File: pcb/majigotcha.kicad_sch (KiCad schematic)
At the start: 11 parts, among them SW1 SW_Push, SW2 SW_Push, SW3 SW_Push, U1 XIAO-ESP32-C6, U2 DM-OLED096-636, U3 TPP233-IC, U4 TOUCH CAPACITIVE

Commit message: finish the pcb
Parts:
- removed U1: XIAO-ESP32-C6, footprints:XIAO-Generic-Hybrid-14P-2.54-21X17.8MM, symbol Seeed_Studio_XIAO_Series:XIAO_ESP32-C6-DIP
- added U5: XIAO-ESP32-S3-SMD, Seeed Studio XIAO Series Library:XIAO-ESP32C6-SMD, symbol Seeed_Studio_XIAO_Series:XIAO-ESP32-C6-SMD
- BT1: footprint (none) -> Connector_PinHeader_2.54mm:PinHeader_1x02_P2.54mm_Vertical
- BUZZER1: footprint buzzer:C49246964_BUZ-TH_BD12_5-P6_50-D1_4 -> Buzzer_Beeper:Buzzer_TDK_PS1240P02BT_D12.2mm_H6.5mm
- SW1, SW2, SW3: footprint Button_Switch_THT:SW_PUSH_6mm -> Button_Switch_THT:SW_PUSH_6mm_H5mm
- U3: value TPP233-IC -> TPP233-capacitive; footprint DFR0299:MODULE_DFR0299 -> DFR0299:TTP223-CAPACITIVE
- U4: footprint sen0348:Untitled -> Connector_PinHeader_2.54mm:PinHeader_1x06_P2.54mm_Vertical
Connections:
- net +3V3: now also U5.12 (3V3)
- net +5V: now also U5.14 (5V)
- net BTN1: now also U5.2 (GPIO1_A1_D1)
- net BTN2: now also U5.1 (GPIO0_A0_D0)
- net BTN3: now also U5.10 (GPIO20_D9_MISO)
- net GND: now also BT1.2 (-), U3.3 (GND), U5.13 (GND), U5.16 (GND); no longer U3.7 (GND)
- net POTENTIO: now also U5.3 (GPIO2_A2_D2)
- net RX: now also U5.8 (GPIO17_D7_RX)
- net SCL: now also U5.6 (GPIO23_D5_SCL)
- net SDA: now also U5.5 (GPIO22_D4_SDA)
- net TOUCH: now also U3.2 (SIG/LOW), U5.4 (GPIO21_D3); no longer U3.9 (SIG/LOW)
- net TOUCH_OUT: now also U5.9 (GPIO19_D8_SCK)
- net TX: now also U5.7 (GPIO16_D6_TX)
- net +BATT: now reaches BT1.1 (+)
- net +BATT: now also U5.15 (BAT); no longer BT1.
- net BUZ: now reaches BUZZER1.1 (+)
- net BUZ: now also U5.11 (GPIO18_D10_MOSI)

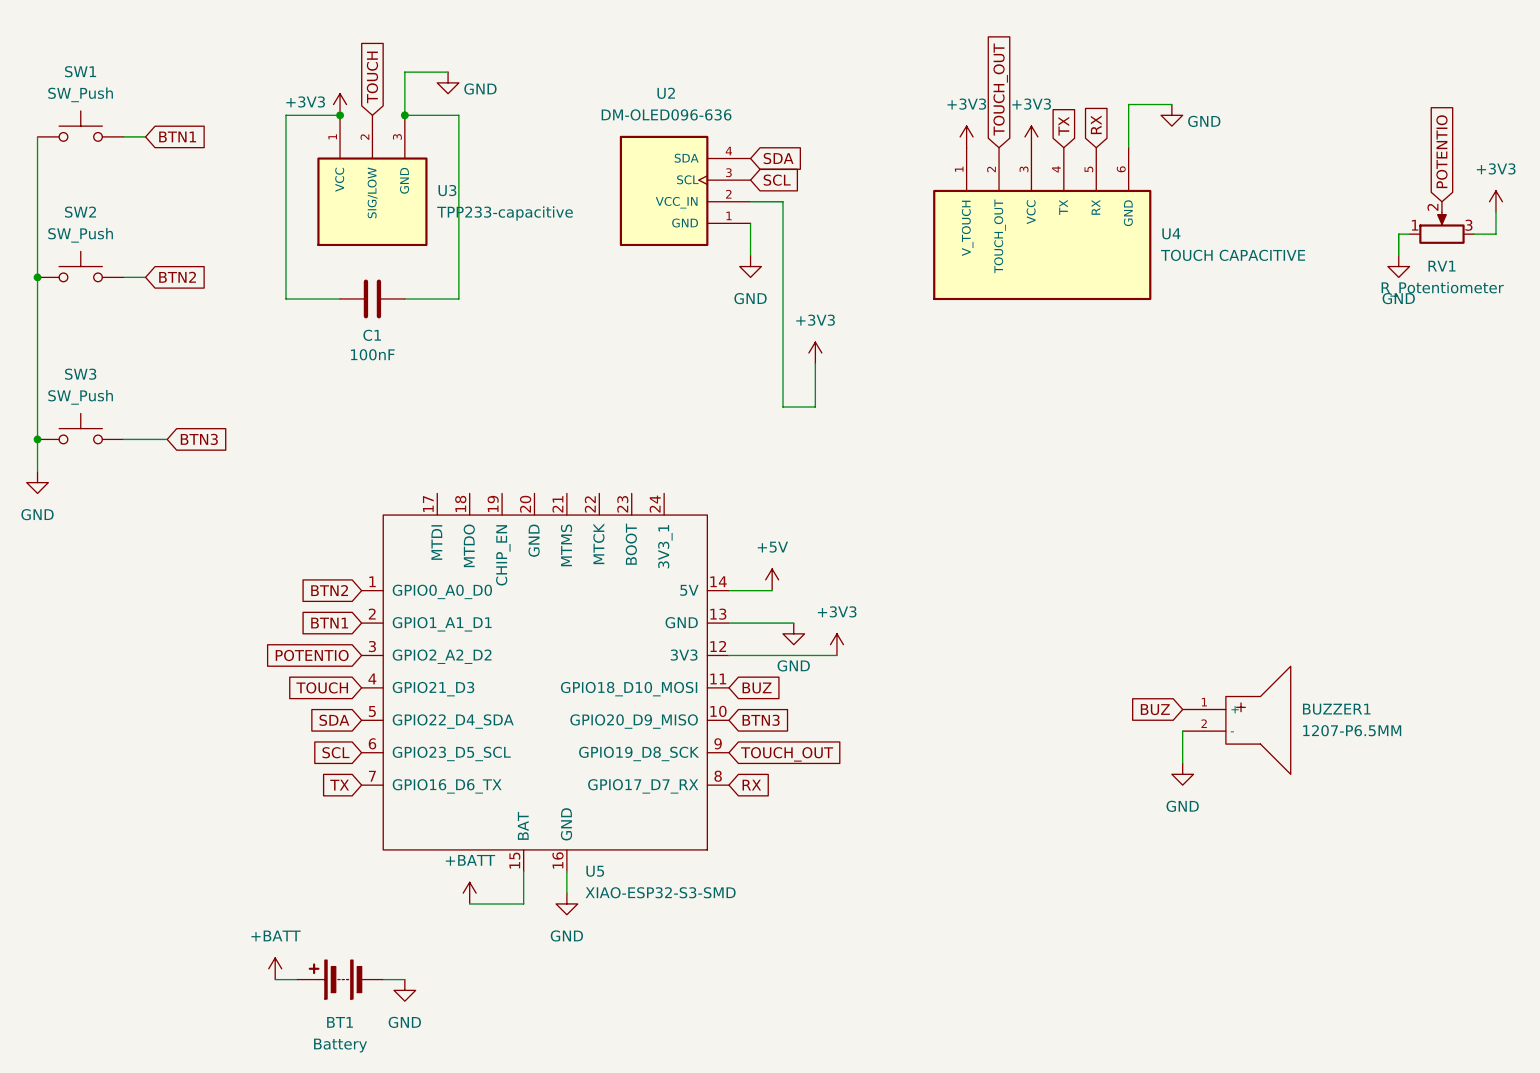
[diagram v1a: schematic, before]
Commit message: add firmware! oh and change of pcb wiring
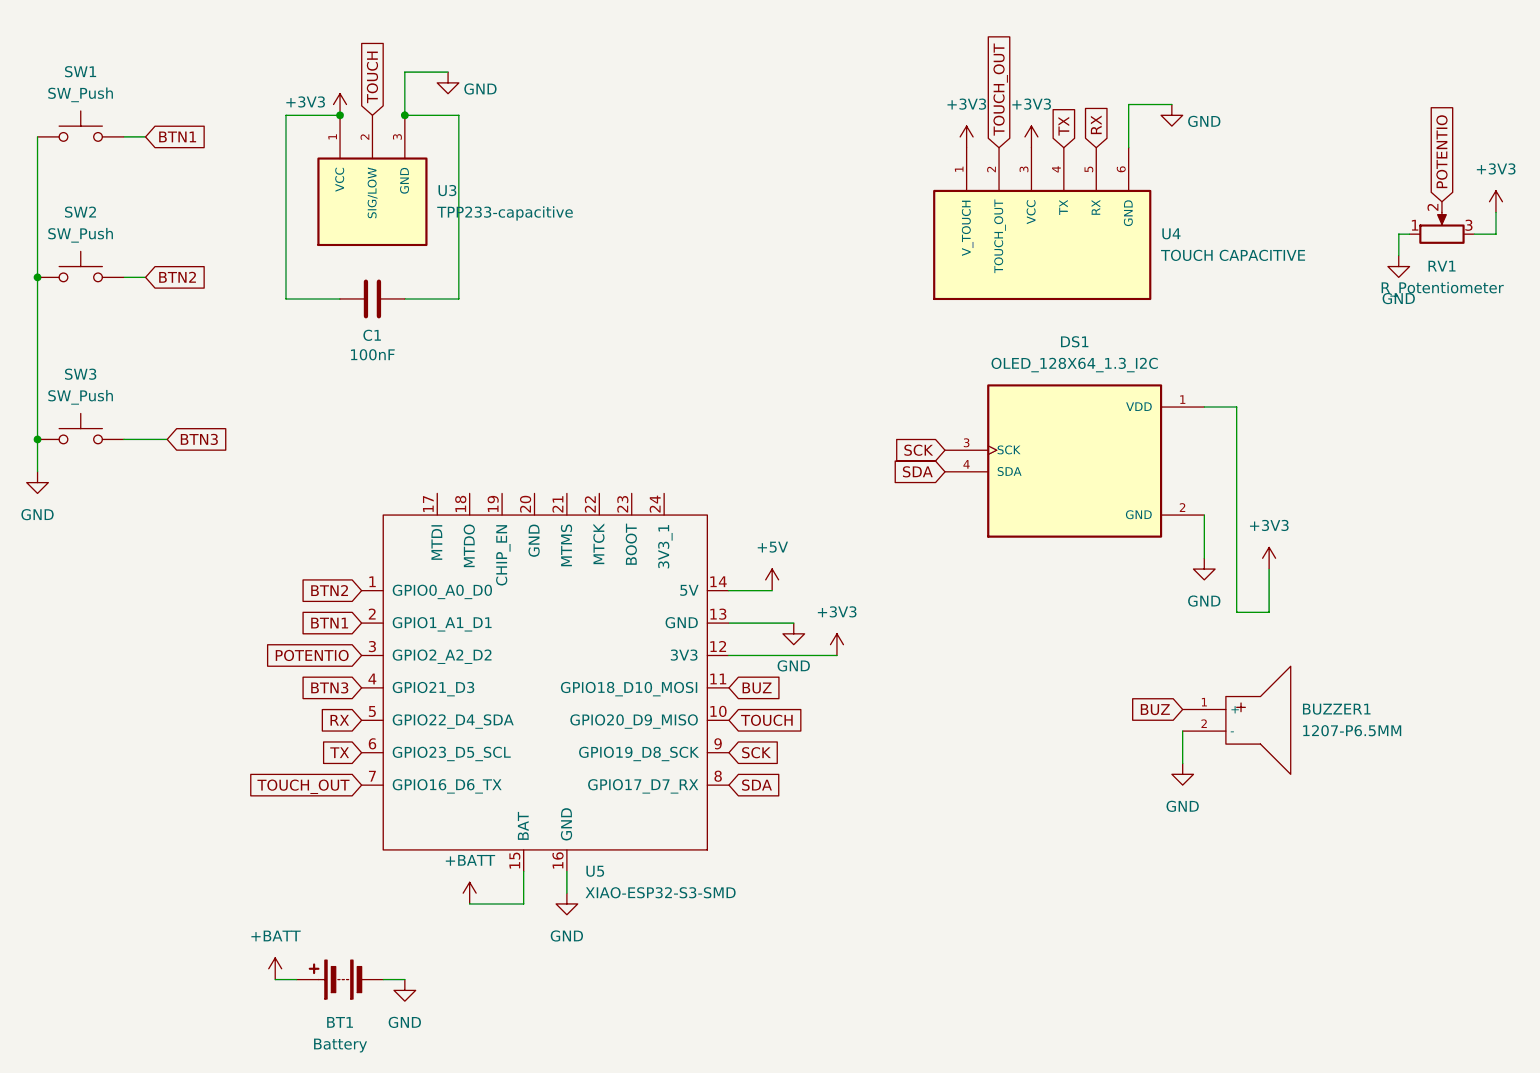
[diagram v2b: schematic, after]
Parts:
- removed U2: DM-OLED096-636, DM-OLED096-636:MODULE_DM-OLED096-636, symbol DM-OLED096-636:DM-OLED096-636
- added DS1: OLED_128X64_1.3_I2C, Connector_PinSocket_2.54mm:PinSocket_1x04_P2.54mm_Vertical, symbol OLED_128X64_1.3_I2C:OLED_128X64_1.3_I2C
- BUZZER1: footprint Buzzer_Beeper:Buzzer_TDK_PS1240P02BT_D12.2mm_H6.5mm -> Connector_PinSocket_2.54mm:PinSocket_1x02_P2.54mm_Vertical
- U3: footprint DFR0299:TTP223-CAPACITIVE -> Connector_PinHeader_2.54mm:PinHeader_1x03_P2.54mm_Vertical
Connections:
- net SCL is gone; now on net TX: U5.6 (GPIO23_D5_SCL)
- net +3V3: now also DS1.1 (VDD)
- net BTN3: now also U5.4 (GPIO21_D3); no longer U5.10 (GPIO20_D9_MISO)
- net GND: now also DS1.2 (GND)
- net RX: now also U5.5 (GPIO22_D4_SDA); no longer U5.8 (GPIO17_D7_RX)
- net SDA: now also U5.8 (GPIO17_D7_RX), DS1.4 (SDA); no longer U5.5 (GPIO22_D4_SDA)
- net TOUCH: now also U5.10 (GPIO20_D9_MISO); no longer U5.4 (GPIO21_D3)
- net TOUCH_OUT: now also U5.7 (GPIO16_D6_TX); no longer U5.9 (GPIO19_D8_SCK)
- net TX: no longer U5.7 (GPIO16_D6_TX)
- new net SCK: DS1.3 (SCK), U5.9 (GPIO19_D8_SCK)

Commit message: update gerbers
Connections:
- net RX: now also U5.9 (GPIO19_D8_SCK); no longer U5.5 (GPIO22_D4_SDA)
- net SCK: now also U5.6 (GPIO23_D5_SCL); no longer U5.9 (GPIO19_D8_SCK)
- net SDA: now also U5.5 (GPIO22_D4_SDA); no longer U5.8 (GPIO17_D7_RX)
- net TX: now also U5.8 (GPIO17_D7_RX); no longer U5.6 (GPIO23_D5_SCL)
